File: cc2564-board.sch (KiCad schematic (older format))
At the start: 57 parts, among them J1 TYPE-C-31-M-12, J2 Conn_ARM_JTAG_SWD_10, J3 Conn_Coaxial, J4 BOOT1, J5 BOOT0, J6 Conn_01x16, J7 Conn_01x16, SW1 SW_Push, U1 LD1117#33, U2 LD1117#18, U3 STM32F103C8Tx, U4 CC2564CRVMR, U5 TXB0104D, Y1 Crystal_GND24_Small, Y2 ECS-260-8-36CKM-TR, Y3 ECS-327MVATX-3-CN-TR

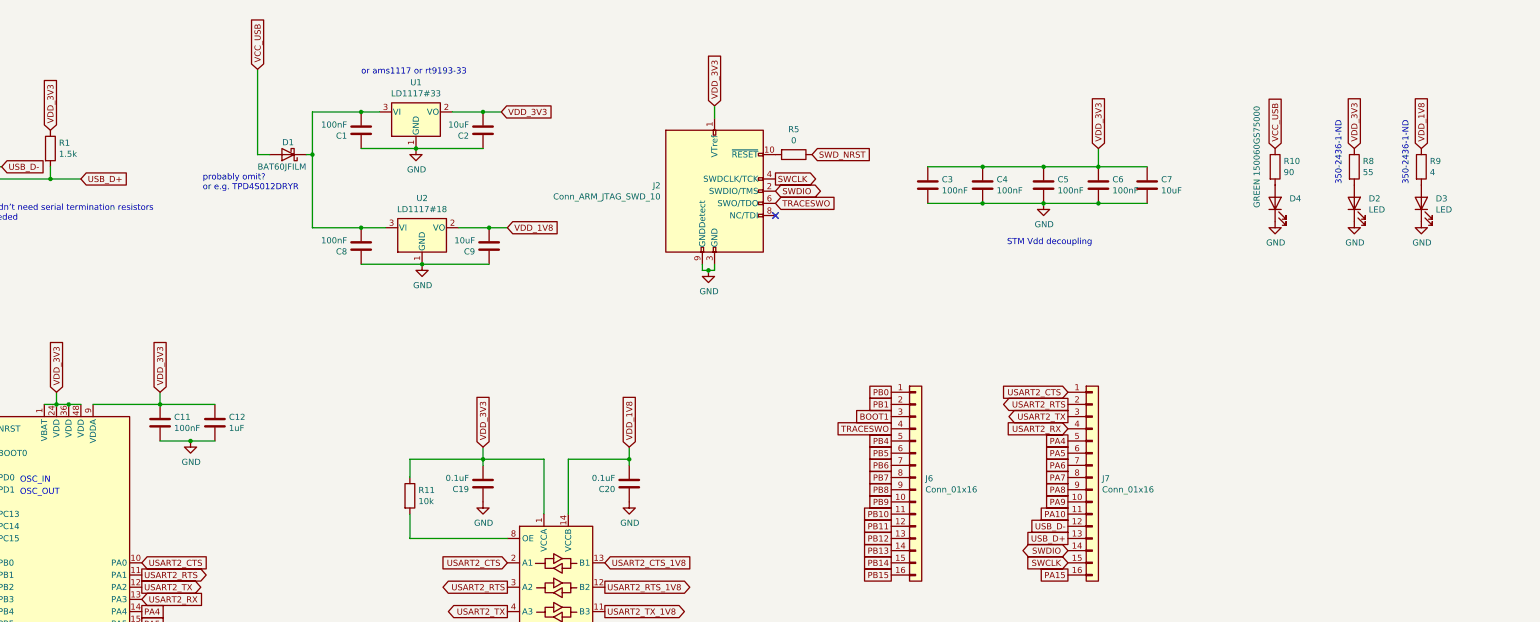
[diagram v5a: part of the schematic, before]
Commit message: Decouple + filter VDDA
Thanks https://www.youtube.com/watch?v=wLwKgMBWhpY
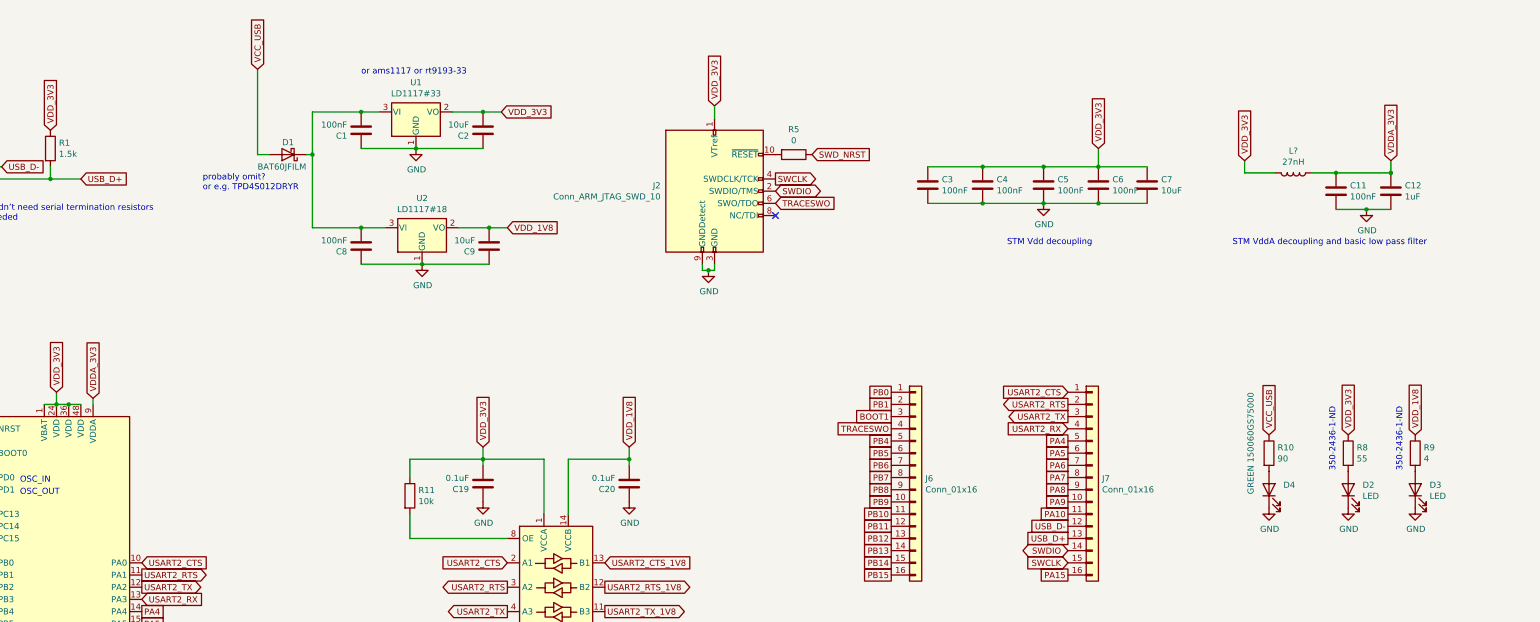
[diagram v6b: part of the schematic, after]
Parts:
- added L?: 27nH, symbol Device:L
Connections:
- net VDD_3V3: now also L?.2; no longer C11.1, C12.1, U3.9 (VDDA)
- new net VDDA_3V3: C11.1, C12.1, L?.1, U3.9 (VDDA)
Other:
- note added: "STM VddA decoupling and basic low pass filter"
- moved on the sheet: C11, C12, D2, D3, D4, R10, R8, R9
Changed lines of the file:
@@
 L Device:LED D4
 U 1 1 5FE2135D
-P 14100 2100
-F 0 "D4" V 14139 1982 50  0000 R CNN
-F 1 "GREEN 150060GS75000" H 14900 2250 50  0000 R CNN
-F 2 "LED_SMD:LED_0603_1608Metric_Pad1.05x0.95mm_HandSolder" H 14100 2100 50  0001 C CNN
-F 3 "~" H 14100 2100 50  0001 C CNN
-	1    14100 2100
+P 14050 4450
+F 0 "D4" V 14089 4332 50  0000 R CNN
+F 1 "GREEN 150060GS75000" H 14850 4600 50  0000 R CNN
+F 2 "LED_SMD:LED_0603_1608Metric_Pad1.05x0.95mm_HandSolder" H 14050 4450 50  0001 C CNN
+F 3 "~" H 14050 4450 50  0001 C CNN
+	1    14050 4450
 	0    -1   -1   0
 $EndComp
@@
 L Device:LED D2
 U 1 1 5FE232B0
-P 14750 2100
-F 0 "D2" V 14789 1982 50  0000 R CNN
-F 1 "LED" V 14698 1982 50  0000 R CNN
-F 2 "LED_SMD:LED_0603_1608Metric_Pad1.05x0.95mm_HandSolder" H 14750 2100 50  0001 C CNN
-F 3 "~" H 14750 2100 50  0001 C CNN
-	1    14750 2100
+P 14700 4450
+F 0 "D2" V 14739 4332 50  0000 R CNN
+F 1 "LED" V 14648 4332 50  0000 R CNN
+F 2 "LED_SMD:LED_0603_1608Metric_Pad1.05x0.95mm_HandSolder" H 14700 4450 50  0001 C CNN
+F 3 "~" H 14700 4450 50  0001 C CNN
+	1    14700 4450
 	0    -1   -1   0
 $EndComp
@@
 L Device:LED D3
 U 1 1 5FE23591
-P 15300 2100
-F 0 "D3" V 15339 1982 50  0000 R CNN
-F 1 "LED" V 15248 1982 50  0000 R CNN
-F 2 "LED_SMD:LED_0603_1608Metric_Pad1.05x0.95mm_HandSolder" H 15300 2100 50  0001 C CNN
-F 3 "~" H 15300 2100 50  0001 C CNN
-	1    15300 2100
+P 15250 4450
+F 0 "D3" V 15289 4332 50  0000 R CNN
+F 1 "LED" V 15198 4332 50  0000 R CNN
+F 2 "LED_SMD:LED_0603_1608Metric_Pad1.05x0.95mm_HandSolder" H 15250 4450 50  0001 C CNN
+F 3 "~" H 15250 4450 50  0001 C CNN
+	1    15250 4450
 	0    -1   -1   0
 $EndComp
@@
 L power:GND #PWR016
 U 1 1 5FE2607F
-P 14100 2250
-F 0 "#PWR016" H 14100 2000 50  0001 C CNN
-F 1 "GND" H 14105 2077 50  0000 C CNN
-F 2 "" H 14100 2250 50  0001 C CNN
-F 3 "" H 14100 2250 50  0001 C CNN
-	1    14100 2250
+P 14050 4600
+F 0 "#PWR016" H 14050 4350 50  0001 C CNN
+F 1 "GND" H 14055 4427 50  0000 C CNN
+F 2 "" H 14050 4600 50  0001 C CNN
+F 3 "" H 14050 4600 50  0001 C CNN
+	1    14050 4600
 	1    0    0    -1
 $EndComp
@@
 L power:GND #PWR014
 U 1 1 5FE264F4
-P 14750 2250
-F 0 "#PWR014" H 14750 2000 50  0001 C CNN
-F 1 "GND" H 14755 2077 50  0000 C CNN
-F 2 "" H 14750 2250 50  0001 C CNN
-F 3 "" H 14750 2250 50  0001 C CNN
-	1    14750 2250
+P 14700 4600
+F 0 "#PWR014" H 14700 4350 50  0001 C CNN
+F 1 "GND" H 14705 4427 50  0000 C CNN
+F 2 "" H 14700 4600 50  0001 C CNN
+F 3 "" H 14700 4600 50  0001 C CNN
+	1    14700 4600
 	1    0    0    -1
 $EndComp
@@
 L power:GND #PWR015
 U 1 1 5FE267D1
-P 15300 2250
-F 0 "#PWR015" H 15300 2000 50  0001 C CNN
-F 1 "GND" H 15305 2077 50  0000 C CNN
-F 2 "" H 15300 2250 50  0001 C CNN
-F 3 "" H 15300 2250 50  0001 C CNN
-	1    15300 2250
+P 15250 4600
+F 0 "#PWR015" H 15250 4350 50  0001 C CNN
+F 1 "GND" H 15255 4427 50  0000 C CNN
+F 2 "" H 15250 4600 50  0001 C CNN
+F 3 "" H 15250 4600 50  0001 C CNN
+	1    15250 4600
 	1    0    0    -1
 $EndComp
@@
 L Device:R R10
 U 1 1 5FE2701E
-P 14100 1800
-F 0 "R10" H 14170 1846 50  0000 L CNN
-F 1 "90" H 14170 1755 50  0000 L CNN
-F 2 "Resistor_SMD:R_0402_1005Metric_Pad0.72x0.64mm_HandSolder" V 14030 1800 50  0001 C CNN
-F 3 "~" H 14100 1800 50  0001 C CNN
-	1    14100 1800
+P 14050 4150
+F 0 "R10" H 14120 4196 50  0000 L CNN
+F 1 "90" H 14120 4105 50  0000 L CNN
+F 2 "Resistor_SMD:R_0402_1005Metric_Pad0.72x0.64mm_HandSolder" V 13980 4150 50  0001 C CNN
+F 3 "~" H 14050 4150 50  0001 C CNN
+	1    14050 4150
 	1    0    0    -1
 $EndComp
@@
 L Device:R R8
 U 1 1 5FE2762F
-P 14750 1800
-F 0 "R8" H 14820 1846 50  0000 L CNN
-F 1 "55" H 14820 1755 50  0000 L CNN
-F 2 "Resistor_SMD:R_0402_1005Metric_Pad0.72x0.64mm_HandSolder" V 14680 1800 50  0001 C CNN
-F 3 "~" H 14750 1800 50  0001 C CNN
-	1    14750 1800
+P 14700 4150
+F 0 "R8" H 14770 4196 50  0000 L CNN
+F 1 "55" H 14770 4105 50  0000 L CNN
+F 2 "Resistor_SMD:R_0402_1005Metric_Pad0.72x0.64mm_HandSolder" V 14630 4150 50  0001 C CNN
+F 3 "~" H 14700 4150 50  0001 C CNN
+	1    14700 4150
 	1    0    0    -1
 $EndComp
@@
 L Device:R R9
 U 1 1 5FE27A79
-P 15300 1800
-F 0 "R9" H 15370 1846 50  0000 L CNN
-F 1 "4" H 15370 1755 50  0000 L CNN
-F 2 "Resistor_SMD:R_0402_1005Metric_Pad0.72x0.64mm_HandSolder" V 15230 1800 50  0001 C CNN
-F 3 "~" H 15300 1800 50  0001 C CNN
-	1    15300 1800
-	1    0    0    -1
-$EndComp
-Text GLabel 14100 1650 1    50   Input ~ 0
+P 15250 4150
+F 0 "R9" H 15320 4196 50  0000 L CNN
+F 1 "4" H 15320 4105 50  0000 L CNN
+F 2 "Resistor_SMD:R_0402_1005Metric_Pad0.72x0.64mm_HandSolder" V 15180 4150 50  0001 C CNN
+F 3 "~" H 15250 4150 50  0001 C CNN
+	1    15250 4150
+	1    0    0    -1
+$EndComp
+Text GLabel 14050 4000 1    50   Input ~ 0
 VCC_USB
-Text GLabel 14750 1650 1    50   Input ~ 0
+Text GLabel 14700 4000 1    50   Input ~ 0
 VDD_3V3
-Text GLabel 15300 1650 1    50   Input ~ 0
+Text GLabel 15250 4000 1    50   Input ~ 0
 VDD_1V8
 Wire Wire Line
@@
 Wire Wire Line
 	13050 2100 12650 2100
-Text GLabel 4950 3650 1    50   Input ~ 0
-VDD_3V3
+Text GLabel 15050 1750 1    50   Input ~ 0
+VDDA_3V3
 $Comp
 L Device:C C12
 U 1 1 5FE40BC0
-P 5400 3900
-F 0 "C12" H 5515 3946 50  0000 L CNN
-F 1 "1uF" H 5515 3855 50  0000 L CNN
-F 2 "Capacitor_SMD:C_0603_1608Metric_Pad1.08x0.95mm_HandSolder" H 5438 3750 50  0001 C CNN
-F 3 "~" H 5400 3900 50  0001 C CNN
-	1    5400 3900
+P 15050 2000
+F 0 "C12" H 15165 2046 50  0000 L CNN
+F 1 "1uF" H 15165 1955 50  0000 L CNN
+F 2 "Capacitor_SMD:C_0603_1608Metric_Pad1.08x0.95mm_HandSolder" H 15088 1850 50  0001 C CNN
+F 3 "~" H 15050 2000 50  0001 C CNN
+	1    15050 2000
 	1    0    0    -1
 $EndComp
@@
 L power:GND #PWR08
 U 1 1 5FE48203
-P 5200 4050
-F 0 "#PWR08" H 5200 3800 50  0001 C CNN
-F 1 "GND" H 5205 3877 50  0000 C CNN
-F 2 "" H 5200 4050 50  0001 C CNN
-F 3 "" H 5200 4050 50  0001 C CNN
-	1    5200 4050
-	1    0    0    -1
-$EndComp
-Wire Wire Line
-	5200 4050 5400 4050
-Connection ~ 4950 3750
+P 14850 2150
+F 0 "#PWR08" H 14850 1900 50  0001 C CNN
+F 1 "GND" H 14855 1977 50  0000 C CNN
+F 2 "" H 14850 2150 50  0001 C CNN
+F 3 "" H 14850 2150 50  0001 C CNN
+	1    14850 2150
+	1    0    0    -1
+$EndComp
+Wire Wire Line
+	14850 2150 15050 2150
+Connection ~ 14600 1850
 Text GLabel 4100 3650 1    50   Input ~ 0
 VDD_3V3
@@
 boot mode select
 Wire Wire Line
-	4400 3750 4950 3750
-Wire Wire Line
-	4950 3750 5400 3750
-Wire Wire Line
-	4950 3650 4950 3750
+	14600 1850 15050 1850
 Connection ~ 4200 3750
 Connection ~ 4100 6750
@@
 L Device:C C11
 U 1 1 5FE40EF5
-P 4950 3900
-F 0 "C11" H 5065 3946 50  0000 L CNN
-F 1 "100nF" H 5065 3855 50  0000 L CNN
-F 2 "Capacitor_SMD:C_0603_1608Metric_Pad1.08x0.95mm_HandSolder" H 4988 3750 50  0001 C CNN
-F 3 "~" H 4950 3900 50  0001 C CNN
-	1    4950 3900
-	1    0    0    -1
-$EndComp
-Wire Wire Line
-	4950 4050 5200 4050
-Connection ~ 5200 4050
+P 14600 2000
+F 0 "C11" H 14715 2046 50  0000 L CNN
+F 1 "100nF" H 14715 1955 50  0000 L CNN
+F 2 "Capacitor_SMD:C_0603_1608Metric_Pad1.08x0.95mm_HandSolder" H 14638 1850 50  0001 C CNN
+F 3 "~" H 14600 2000 50  0001 C CNN
+	1    14600 2000
+	1    0    0    -1
+$EndComp
+Wire Wire Line
+	14600 2150 14850 2150
+Connection ~ 14850 2150
 Wire Wire Line
 	8850 11650 9200 11650
@@
 Text GLabel 11150 6250 0    50   Input ~ 0
 GND
-Text Notes 14650 1950 1    50   ~ 0
+Text Notes 14600 4300 1    50   ~ 0
 350-2436-1-ND‎
-Text Notes 15200 1950 1    50   ~ 0
+Text Notes 15150 4300 1    50   ~ 0
 350-2436-1-ND‎
 Text GLabel 3650 1800 2    50   Input ~ 0
 USB_D-
+Text GLabel 4400 3700 1    50   Input ~ 0
+VDDA_3V3
+Wire Wire Line
+	4400 3700 4400 3750
+Text GLabel 13850 1750 1    50   Input ~ 0
+VDD_3V3
+$Comp
+L Device:L L?
+U 1 1 60892857
+P 14250 1850
+F 0 "L?" V 14069 1850 50  0000 C CNN
+F 1 "27nH" V 14160 1850 50  0000 C CNN
+F 2 "" H 14250 1850 50  0001 C CNN
+F 3 "~" H 14250 1850 50  0001 C CNN
+	1    14250 1850
+	0    1    1    0
+$EndComp
+Wire Wire Line
+	13850 1750 13850 1850
+Wire Wire Line
+	13850 1850 14100 1850
+Wire Wire Line
+	14400 1850 14600 1850
+Text Notes 13750 2450 0    50   ~ 0
+STM VddA decoupling and basic low pass filter
+Wire Wire Line
+	15050 1750 15050 1850
+Connection ~ 15050 1850
 $EndSCHEMATC

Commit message: Filter BT slow clock osc power input per datasheet
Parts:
- removed C23: 0.1uF, Capacitor_SMD:C_0603_1608Metric_Pad1.08x0.95mm_HandSolder, symbol Device:C
- added C? (x2): 1uF, Capacitor_SMD:C_0603_1608Metric_Pad1.08x0.95mm_HandSolder, symbol Device:C
- added C? (x3): 0.1uF, Capacitor_SMD:C_0603_1608Metric_Pad1.08x0.95mm_HandSolder, symbol Device:C
- added C? (x2): 0.47uF, Capacitor_SMD:C_0603_1608Metric_Pad1.08x0.95mm_HandSolder, symbol Device:C
- added FB?: BK1005HS680-T‎, symbol Device:Ferrite_Bead
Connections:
- net GND: now also C?.2, C?.2, C?.2, C?.2, C?.2, C?.2, C?.2
- net VDD_1V8: now also FB?.2; no longer R12.1, Y3.4 (VDD)
- net DIG_LDO_OUT: now reaches U4.A2 (DIG_LDO_OUT)
- net DIG_LDO_OUT: now also U4.A3 (DIG_LDO_OUT), U4.B15 (DIG_LDO_OUT), U4.B26 (DIG_LDO_OUT), U4.B27 (DIG_LDO_OUT), U4.B35 (DIG_LDO_OUT), U4.B36 (DIG_LDO_OUT), C?.1, C?.1, C?.1, C?.1
- net MLDO_OUT: now reaches U4.A5 (MLDO_OUT)
- net MLDO_OUT: now also U4.A9 (MLDO_OUT), U4.B2 (MLDO_OUT), U4.B7 (MLDO_OUT), C?.1, C?.1
- new net VDD_1V8_32K: C?.1, FB?.1, R12.1, Y3.4 (VDD)
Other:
- note added: "68ohm @ 100MHz"
- note added: "CC2564 slow clk oscillator decoupling and filtering"
- note added: "probably omit?\nor e.g. TPD4S012DRYR,\nUSBLC6-2P6"
- note removed: "probably omit?\nor e.g. TPD4S012DRYR"
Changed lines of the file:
@@
 Wire Wire Line
 	13050 2100 12650 2100
-Text GLabel 15050 1750 1    50   Input ~ 0
+Text GLabel 15150 1850 2    50   Input ~ 0
 VDDA_3V3
 $Comp
@@
 Wire Wire Line
 	6150 1700 6200 1700
-Text Notes 5300 2000 0    50   ~ 0
-probably omit?\nor e.g. TPD4S012DRYR
+Text Notes 5300 2100 0    50   ~ 0
+probably omit?\nor e.g. TPD4S012DRYR,\nUSBLC6-2P6
 $Comp
 L Device:D_Schottky D1
@@
 	1    0    0    -1
 $EndComp
-$Comp
-L Device:C C23
-U 1 1 60632F1C
-P 2600 12800
-F 0 "C23" H 2715 12846 50  0000 L CNN
-F 1 "0.1uF" H 2715 12755 50  0000 L CNN
-F 2 "Capacitor_SMD:C_0603_1608Metric_Pad1.08x0.95mm_HandSolder" H 2638 12650 50  0001 C CNN
-F 3 "~" H 2600 12800 50  0001 C CNN
-	1    2600 12800
-	1    0    0    -1
-$EndComp
-Wire Wire Line
-	2600 12650 3050 12650
-Text GLabel 2600 12000 1    50   Input ~ 0
-VDD_1V8
-Connection ~ 2600 12650
-Wire Wire Line
-	2600 12000 2600 12150
+Wire Wire Line
+	2850 12650 3050 12650
+Text GLabel 2850 12100 1    50   Input ~ 0
+VDD_1V8_32K
+Wire Wire Line
+	2850 12100 2850 12150
 Wire Wire Line
 	3050 12850 3000 12850
@@
 	3000 12850 3000 12550
 Wire Wire Line
-	3000 12150 2600 12150
-Connection ~ 2600 12150
-Wire Wire Line
-	2600 12150 2600 12650
-$Comp
-L power:GND #PWR0107
-U 1 1 6066FBF6
-P 2600 13000
-F 0 "#PWR0107" H 2600 12750 50  0001 C CNN
-F 1 "GND" H 2605 12827 50  0000 C CNN
-F 2 "" H 2600 13000 50  0001 C CNN
-F 3 "" H 2600 13000 50  0001 C CNN
-	1    2600 13000
-	1    0    0    -1
-$EndComp
-Wire Wire Line
-	2600 13000 2600 12950
+	3000 12150 2850 12150
+Connection ~ 2850 12150
+Wire Wire Line
+	2850 12150 2850 12650
 Wire Wire Line
 	4650 13050 4650 13100
@@
 STM VddA decoupling and basic low pass filter
 Wire Wire Line
-	15050 1750 15050 1850
+	15150 1850 15050 1850
 Connection ~ 15050 1850
+Wire Wire Line
+	8300 12650 8300 12750
+Connection ~ 8300 12750
+Wire Wire Line
+	8300 12750 8300 12850
+Connection ~ 8300 12850
+Wire Wire Line
+	8300 12850 8300 12950
+$Comp
+L Device:C C?
+U 1 1 6090E478
+P 8550 12800
+F 0 "C?" H 8665 12846 50  0000 L CNN
+F 1 "1uF" H 8665 12755 50  0000 L CNN
+F 2 "Capacitor_SMD:C_0603_1608Metric_Pad1.08x0.95mm_HandSolder" H 8588 12650 50  0001 C CNN
+F 3 "~" H 8550 12800 50  0001 C CNN
+	1    8550 12800
+	1    0    0    -1
+$EndComp
+$Comp
+L Device:C C?
+U 1 1 6090F3F2
+P 8950 12800
+F 0 "C?" H 9065 12846 50  0000 L CNN
+F 1 "1uF" H 9065 12755 50  0000 L CNN
+F 2 "Capacitor_SMD:C_0603_1608Metric_Pad1.08x0.95mm_HandSolder" H 8988 12650 50  0001 C CNN
+F 3 "~" H 8950 12800 50  0001 C CNN
+	1    8950 12800
+	1    0    0    -1
+$EndComp
+$Comp
+L power:GND #PWR?
+U 1 1 60924A2D
+P 8950 12950
+F 0 "#PWR?" H 8950 12700 50  0001 C CNN
+F 1 "GND" H 8955 12777 50  0000 C CNN
+F 2 "" H 8950 12950 50  0001 C CNN
+F 3 "" H 8950 12950 50  0001 C CNN
+	1    8950 12950
+	1    0    0    -1
+$EndComp
+Connection ~ 8950 12950
+Wire Wire Line
+	8550 12650 8950 12650
+Wire Wire Line
+	8550 12950 8950 12950
+Wire Wire Line
+	8300 12650 8550 12650
+Connection ~ 8300 12650
+Connection ~ 8550 12650
+Wire Wire Line
+	8300 13650 8300 13750
+Connection ~ 8300 13750
+Wire Wire Line
+	8300 13750 8300 13850
+Connection ~ 8300 13850
+Wire Wire Line
+	8300 13850 8300 13950
+Connection ~ 8300 13950
+Wire Wire Line
+	8300 13950 8300 14050
+Connection ~ 8300 14050
+Wire Wire Line
+	8300 14050 8300 14150
+Connection ~ 8300 14150
+Wire Wire Line
+	8300 14150 8300 14250
+$Comp
+L Device:C C?
+U 1 1 609A9635
+P 8550 13800
+F 0 "C?" H 8665 13846 50  0000 L CNN
+F 1 "0.1uF" H 8665 13755 50  0000 L CNN
+F 2 "Capacitor_SMD:C_0603_1608Metric_Pad1.08x0.95mm_HandSolder" H 8588 13650 50  0001 C CNN
+F 3 "~" H 8550 13800 50  0001 C CNN
+	1    8550 13800
+	1    0    0    -1
+$EndComp
+$Comp
+L Device:C C?
+U 1 1 609A963B
+P 9050 13800
+F 0 "C?" H 9165 13846 50  0000 L CNN
+F 1 "0.1uF" H 9165 13755 50  0000 L CNN
+F 2 "Capacitor_SMD:C_0603_1608Metric_Pad1.08x0.95mm_HandSolder" H 9088 13650 50  0001 C CNN
+F 3 "~" H 9050 13800 50  0001 C CNN
+	1    9050 13800
+	1    0    0    -1
+$EndComp
+$Comp
+L power:GND #PWR?
+U 1 1 609A9641
+P 9050 13950
+F 0 "#PWR?" H 9050 13700 50  0001 C CNN
+F 1 "GND" H 9055 13777 50  0000 C CNN
+F 2 "" H 9050 13950 50  0001 C CNN
+F 3 "" H 9050 13950 50  0001 C CNN
+	1    9050 13950
+	1    0    0    -1
+$EndComp
+Connection ~ 9050 13950
+Wire Wire Line
+	8300 13650 8550 13650
+Wire Wire Line
+	8550 13950 9050 13950
+Wire Wire Line
+	8550 13650 9050 13650
+Connection ~ 8550 13650
+$Comp
+L Device:C C?
+U 1 1 609D9FCB
+P 9550 13800
+F 0 "C?" H 9665 13846 50  0000 L CNN
+F 1 "0.47uF" H 9665 13755 50  0000 L CNN
+F 2 "Capacitor_SMD:C_0603_1608Metric_Pad1.08x0.95mm_HandSolder" H 9588 13650 50  0001 C CNN
+F 3 "~" H 9550 13800 50  0001 C CNN
+	1    9550 13800
+	1    0    0    -1
+$EndComp
+$Comp
+L Device:C C?
+U 1 1 609DAA99
+P 10100 13800
+F 0 "C?" H 10215 13846 50  0000 L CNN
+F 1 "0.47uF" H 10215 13755 50  0000 L CNN
+F 2 "Capacitor_SMD:C_0603_1608Metric_Pad1.08x0.95mm_HandSolder" H 10138 13650 50  0001 C CNN
+F 3 "~" H 10100 13800 50  0001 C CNN
+	1    10100 13800
+	1    0    0    -1
+$EndComp
+Wire Wire Line
+	9050 13950 9550 13950
+Connection ~ 9550 13950
+Wire Wire Line
+	9550 13950 10100 13950
+Wire Wire Line
+	10350 13650 10100 13650
+Connection ~ 9050 13650
+Connection ~ 9550 13650
+Wire Wire Line
+	9550 13650 9050 13650
+Text GLabel 10350 13650 2    50   Input ~ 0
+DIG_LDO_OUT
+Text GLabel 9200 12650 2    50   Input ~ 0
+MLDO_OUT
+Connection ~ 8950 12650
+Wire Wire Line
+	8950 12650 9200 12650
+Connection ~ 10100 13650
+Wire Wire Line
+	10100 13650 9550 13650
+Text GLabel 16950 1850 2    50   Input ~ 0
+VDD_1V8_32K
+$Comp
+L power:GND #PWR?
+U 1 1 60A125D3
+P 16850 2150
+F 0 "#PWR?" H 16850 1900 50  0001 C CNN
+F 1 "GND" H 16855 1977 50  0000 C CNN
+F 2 "" H 16850 2150 50  0001 C CNN
+F 3 "" H 16850 2150 50  0001 C CNN
+	1    16850 2150
+	1    0    0    -1
+$EndComp
+Connection ~ 16850 1850
+Wire Wire Line
+	16850 1850 16950 1850
+$Comp
+L Device:C C?
+U 1 1 60A125DC
+P 16850 2000
+F 0 "C?" H 16965 2046 50  0000 L CNN
+F 1 "0.1uF" H 16965 1955 50  0000 L CNN
+F 2 "Capacitor_SMD:C_0603_1608Metric_Pad1.08x0.95mm_HandSolder" H 16888 1850 50  0001 C CNN
+F 3 "~" H 16850 2000 50  0001 C CNN
+	1    16850 2000
+	1    0    0    -1
+$EndComp
+Text GLabel 16100 1750 1    50   Input ~ 0
+VDD_1V8
+Wire Wire Line
+	16100 1750 16100 1850
+Wire Wire Line
+	16100 1850 16350 1850
+Wire Wire Line
+	16650 1850 16850 1850
+Text Notes 16000 2450 0    50   ~ 0
+CC2564 slow clk oscillator decoupling and filtering
+$Comp
+L Device:Ferrite_Bead FB?
+U 1 1 60A37906
+P 16500 1850
+F 0 "FB?" V 16226 1850 50  0000 C CNN
+F 1 "BK1005HS680-T‎" V 16317 1850 50  0000 C CNN
+F 2 "" V 16430 1850 50  0001 C CNN
+F 3 "~" H 16500 1850 50  0001 C CNN
+	1    16500 1850
+	0    1    1    0
+$EndComp
+Text Notes 16000 2100 0    50   ~ 0
+68ohm @ 100MHz
 $EndSCHEMATC

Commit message: Add USBLC6 for USB ESD protection
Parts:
- removed D1: BAT60JFILM, symbol Device:D_Schottky
- removed R1: 1.5k, Resistor_SMD:R_0402_1005Metric_Pad0.72x0.64mm_HandSolder, symbol Device:R
- removed R3, R4: 0, Resistor_SMD:R_0402_1005Metric_Pad0.72x0.64mm_HandSolder, symbol Device:R
- added R?: 1.5k, Resistor_SMD:R_0402_1005Metric_Pad0.72x0.64mm_HandSolder, symbol Device:R
- added R? (x2): 0, Resistor_SMD:R_0402_1005Metric_Pad0.72x0.64mm_HandSolder, symbol Device:R
- added U?: USBLC6-2P6, Package_TO_SOT_SMD:SOT-666, symbol Power_Protection:USBLC6-2P6
- FB1: renamed from FB?; footprint (none) -> Inductor_SMD:L_0402_1005Metric_Pad0.77x0.64mm_HandSolder
- L1: renamed from L?; footprint (none) -> Inductor_SMD:L_0402_1005Metric_Pad0.77x0.64mm_HandSolder
- R11, R12, R13: footprint (none) -> Resistor_SMD:R_0402_1005Metric_Pad0.72x0.64mm_HandSolder
- Y3: footprint OSC_ECS-2333-160-BN-TR -> cc2654-board-footprints:OSC_ECS-2333-160-BN-TR
- gave numbers to parts that had none: 7
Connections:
- net GND: now also U?.2 (GND)
- net USB_D+: now also R?.1, R?.2, U?.3 (I/O2); no longer U3.33 (PA12)
- net USB_D-: now also R?.2, U?.1 (I/O1); no longer U3.32 (PA11)
- net VCC_USB: now also C1.2, C8.2, U1.3 (VI), U2.3 (VI), U?.5 (VBUS)
- net VDD_3V3: now also R?.1
- net USB_CONN_D+: now reaches J1.A6 (DP1), J1.B6 (DP2)
- net USB_CONN_D+: now also U?.4 (I/O2)
- net USB_CONN_D-: now reaches J1.A7 (DN1), J1.B7 (DN2)
- net USB_CONN_D-: now also U?.6 (I/O1)
- new net: R?.1, U3.32 (PA11)
- new net: R?.2, U3.33 (PA12)
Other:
- note added: "stm32 shouldn’t need series termination resistors\n22ohm if needed"
- note removed: "probably omit?\nor e.g. TPD4S012DRYR,\nUSBLC6-2P6"
- note removed: "stm32 shouldn’t need serial termination resistors\n22ohm if needed"
- moved on the sheet: C1, C11, C12, C2, C23, C3, C4, C5, C6, C7, C8, C9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
